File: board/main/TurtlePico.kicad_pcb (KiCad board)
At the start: 2 copper layers, 63.5 x 69.3 mm, 46 parts, among them IC1 DRV8835DSSR, J1 USB-C, J10 LMotor, J11 Micro_SD, J12 FR_ESC, J13 FL_ESC, J14 RR_ESC, J15 RL_ESC, J2 AudioJack3, J3 LED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

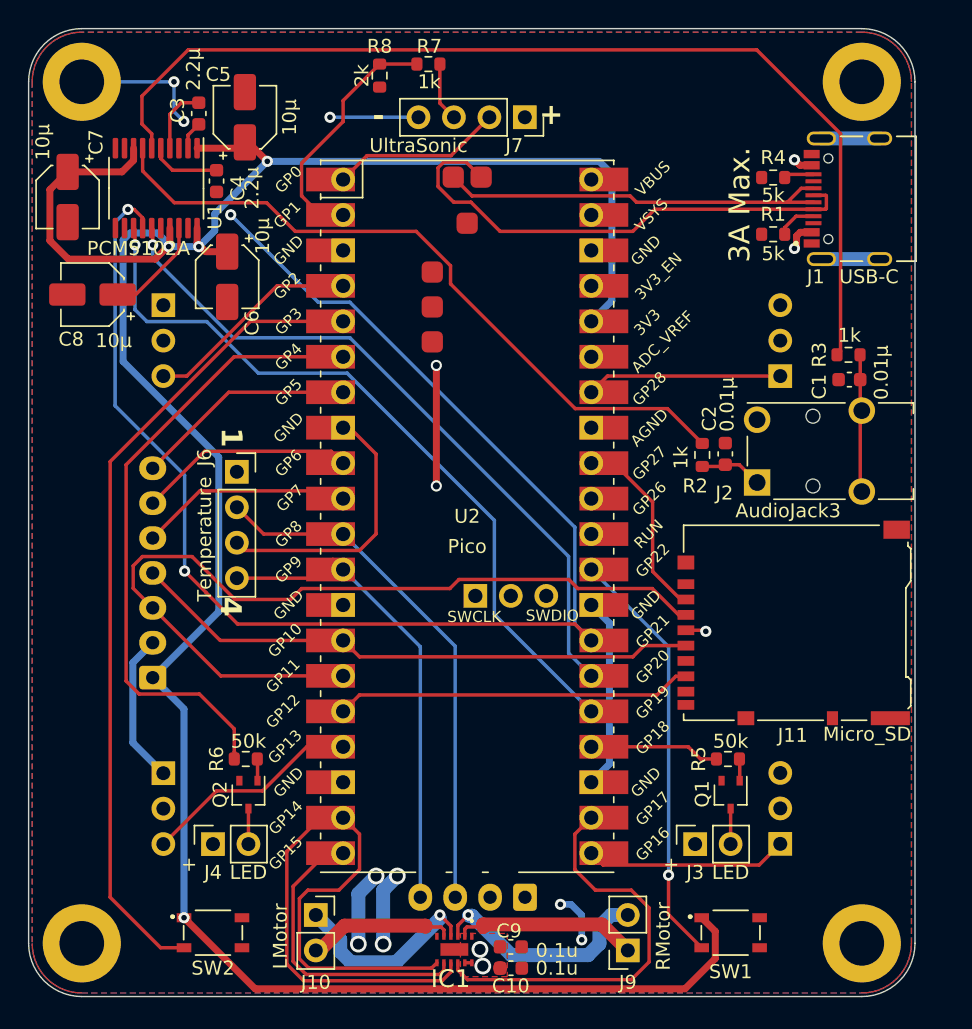
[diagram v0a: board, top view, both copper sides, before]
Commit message: add clock function(only digital) in TurtlePico-Dashboard
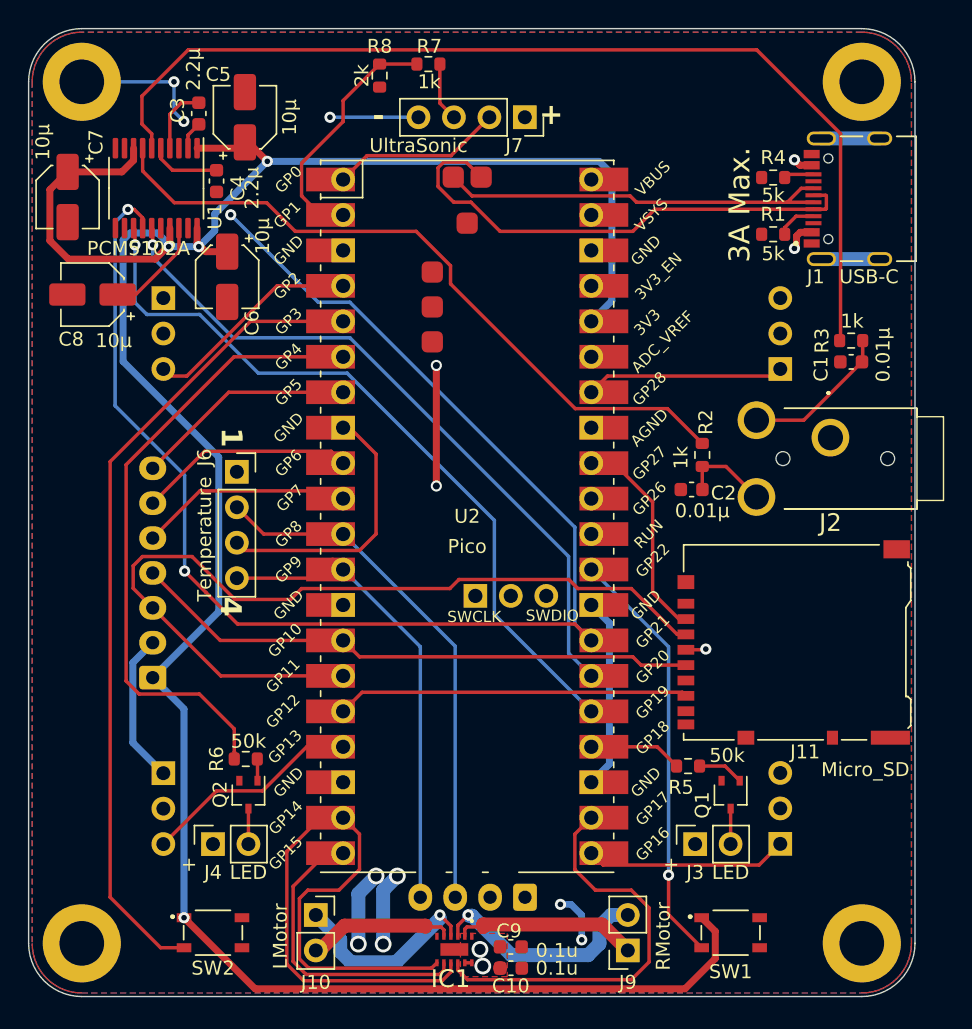
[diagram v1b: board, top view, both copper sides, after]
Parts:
- J2: footprint Connector_Audio:Jack_3.5mm_Switronic_ST-005-G_horizontal -> STX-3000:STX3000
- moved C2 3.51 mm to (161.5, 94.0), turned to 180 degrees
- moved R5 2.90 mm to (161.3, 113.8)
- moved J2 1.58 mm to (171.5, 90.3)
- moved J11 1.40 mm to (168.9, 104.9)
- moved C1 1.28 mm to (173.0, 84.8)
- moved R3 1.03 mm to (173.0, 83.3)
- moved J12 0.51 mm to (167.9, 85.3)
- moved J13 0.51 mm to (123.7, 80.3)
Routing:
- net /GP18: track 9.33 -> 6.68 mm
- net Net-(C2-Pad1): track 4.51 -> 6.44 mm
- net Net-(Q1-B): track 1.56 -> 3.31 mm
- net /GP27: track 13.7 -> 15.2 mm
- net Net-(U1-OUTL): track 73.9 -> 72.8 mm
- net Net-(C1-Pad1): track 10.0 -> 10.9 mm
- net /GP11: track 62.0 -> 62.6 mm
